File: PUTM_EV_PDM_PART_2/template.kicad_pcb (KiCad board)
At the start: 4 copper layers, 60 x 90 mm, 7 parts, among them J3 Conn_02x18_Counter_Clockwise, J4 WIRE OUT, J5 Conn_01x37

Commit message: Add files via upload
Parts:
- removed J5: Conn_01x37, 3RD_party:37 PIN DEUTSCH
- added J1: +24V IN, DPT13-4P:TE_DTP13-4P, F.Cu at (103.0, 103.5)
- added J2: UPS-08-07.0-01-L-V, UPT-08-07-01-L-V:UPS0807001LV, F.Cu at (154.8, 78.5)
- added J6: +24V OUT, UPT-02-01-01-L-V:SAMTEC_UPT-02-03.0-XX-X-V, F.Cu at (156.2, 121.7)
- added J7: UPS-08-07.0-01-L-V, UPT-08-07-01-L-V:UPS0807001LV, F.Cu at (154.8, 39.3)
- J3: footprint Connector_IDC:IDC-Header_2x20-1MP_P2.54mm_Latch6.5mm_Vertical -> 3RD_party:37 PIN DEUTSCH
- J4: value WIRE OUT -> Conn_01x06_Pin; footprint Connector_Wire:SolderWire-0.75sqmm_1x02_P4.8mm_D1.25mm_OD2.3mm_Relief -> Connector_IDC:IDC-Header_2x03_P2.54mm_Vertical
- moved J4 102.5 mm to (123.3, 32.0), turned to -90 degrees
- moved J3 56.7 mm to (121.4, 55.1)
- moved xd1 54.1 mm to (142.5, 35.0)
- moved xd2 49.0 mm to (104.0, 35.0)
- moved xd4 44.2 mm to (143.5, 125.5)
- moved xd3 39.1 mm to (105.2, 125.0)
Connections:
- J3 pad 15: /DASH 24VDC -> /BRAKE BALANCE 24VDC
- J3 pad 17: /PC 24VDC 4 -> /PC 24VDC 3
- J3 pad 19: /TSAL LOGIC 24VDC -> /BSPD 24VDC
- J3 pad 20: /TSAL LIGHT 24VDC -> /BSPD 24VDC
- J3 pad 21: /DIAGPORT 24VDC -> /AIR PRESSURE 24VDC
- J3 pad 22: /IR CAMS REAR 24VDC -> /AIR PRESSURE 24VDC
- J3 pad 24: /ODRIVE 3 24VDC -> /ODRIVE 2 24VDC
- J3 pad 26: /ODRIVE 5 24VDC -> /ODRIVE 4 24VDC
- J3 pad 27: /PC 24VDC 2 -> /PC 24VDC 1
- J3 pad 28: /FRONT BOX 24VDC -> /BRAKE BALANCE 24VDC
- J3 pad 3: /REARBOX 2 24VDC -> /REARBOX 1 24VDC
- J3 pad 30: /INVERTER 2 24VDC -> /INVERTER 1 24VDC
- J3 pad 33: /HV LOGIKA 2 24VDC -> /HV LOGIKA 1 24VDC
- J3 pad 6: /IR CAMS FRONT 24VDC -> /AIR PRESSURE 24VDC
- J3 pad 8: /REARBOX 4 24VDC -> /REARBOX 3 24VDC
- J3 pad 9: /SDC SOURCE -> /ASMS SOURCE
- J4 pad 1: /+24V -> /CAN_L
- J4 pad 2: /GND -> /CAN_H
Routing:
- added copper zone on In1.Cu, net (none)
- added copper zone on In2.Cu, net (none)
- added copper zone on F.Cu, net /AIR PRESSURE 24VDC
- added copper zone on In2.Cu, net /ASMS IN
- added copper zone on In2.Cu, net /ASMS SOURCE
- added copper zone on F.Cu, net /BRAKE BALANCE 24VDC
- added copper zone on In1.Cu, net /CAN_L
- added copper zone on B.Cu, net /ODRIVE 4 24VDC
- removed copper zone on B.Cu, net /ASMS IN
- removed copper zone on F.Cu, net /ASMS IN
- removed copper zone on F.Cu, net /ASMS SOURCE
- removed copper zone on B.Cu, net /CAN_H
- removed copper zone on B.Cu, net /CAN_L
- removed copper zone on F.Cu, net /DASH 24VDC
- removed copper zone on F.Cu, net /DIAGPORT 24VDC
- removed copper zone on F.Cu, net /HV LOGIKA 1 24VDC
- removed copper zone on B.Cu, net /ODRIVE 2 24VDC
- removed copper zone on B.Cu, net /ODRIVE 5 24VDC
- removed copper zone on F.Cu, net /PC 24VDC 1
- removed copper zone on B.Cu, net /REARBOX 1 24VDC
- removed copper zone on B.Cu, net /REARBOX 3 24VDC
- removed copper zone on B.Cu, net /REARBOX 5 24VDC
- removed copper zone on B.Cu, net /TSAL LIGHT 24VDC
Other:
- board size 60 x 90 mm -> 60 x 100 mm

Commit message: Add files via upload
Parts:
- removed J1: +24V IN, DPT13-4P:TE_DTP13-4P
- removed J6: +24V OUT, UPT-02-01-01-L-V:SAMTEC_UPT-02-03.0-XX-X-V
- added J5: +24V OUT, UPT-02-01-01-L-V:SAMTEC_UPT-02-03.0-XX-X-V, F.Cu at (154.1, 119.1)
- added J8: +24V IN, DPT13-4P:TE_DTP13-4P, F.Cu at (107.4, 101.6)
- J4: value Conn_01x06_Pin -> Conn_01x06
- moved J7 3.12 mm to (153.8, 36.3)
- moved J2 2.93 mm to (153.8, 75.8)
- moved xd4 1.84 mm to (141.8, 126.2)
- moved xd1 1.12 mm to (142.0, 34.0)
- moved J4 0.10 mm to (123.4, 32.1)
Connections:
- J2 pad G1: /INVERTER 1 24VDC -> /PC 24VDC 3
- J2 pad G2: /INVERTER 1 24VDC -> /PC 24VDC 3
- J2 pad G3: /INVERTER 1 24VDC -> /PC 24VDC 3
- J2 pad G4: /INVERTER 1 24VDC -> /PC 24VDC 3
- J2 pad G5: /INVERTER 1 24VDC -> /PC 24VDC 3
- J2 pad G6: /INVERTER 1 24VDC -> /PC 24VDC 3
- J2 pad H1: /PC 24VDC 3 -> /INVERTER 1 24VDC
- J2 pad H2: /PC 24VDC 3 -> /INVERTER 1 24VDC
- J2 pad H3: /PC 24VDC 3 -> /INVERTER 1 24VDC
- J2 pad H4: /PC 24VDC 3 -> /INVERTER 1 24VDC
- J2 pad H5: /PC 24VDC 3 -> /INVERTER 1 24VDC
- J2 pad H6: /PC 24VDC 3 -> /INVERTER 1 24VDC
- J7 pad F1: /ODRIVE 2 24VDC -> /PC 24VDC 5
- J7 pad F2: /ODRIVE 2 24VDC -> /PC 24VDC 5
- J7 pad F3: /ODRIVE 2 24VDC -> /PC 24VDC 5
- J7 pad F4: /ODRIVE 2 24VDC -> /PC 24VDC 5
- J7 pad F5: /ODRIVE 2 24VDC -> /PC 24VDC 5
- J7 pad F6: /ODRIVE 2 24VDC -> /PC 24VDC 5
- J7 pad G1: /PC 24VDC 5 -> /ODRIVE 2 24VDC
- J7 pad G2: /PC 24VDC 5 -> /ODRIVE 2 24VDC
- J7 pad G3: /PC 24VDC 5 -> /ODRIVE 2 24VDC
- J7 pad G4: /PC 24VDC 5 -> /ODRIVE 2 24VDC
- J7 pad G5: /PC 24VDC 5 -> /ODRIVE 2 24VDC
- J7 pad G6: /PC 24VDC 5 -> /ODRIVE 2 24VDC
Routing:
- added copper zone on F.Cu, net /+24V
- added copper zone on F.Cu, net /ASMS SOURCE
- added copper zone on B.Cu, net /BSPD 24VDC
- added copper zone on In2.Cu, net /CAN_H
- added copper zone on F.Cu, net /GND
- added copper zone on B.Cu, net /HV LOGIKA 1 24VDC
- added copper zone on In1.Cu, net /ODRIVE 2 24VDC
- added copper zone on F.Cu, net /PC 24VDC 1
- added copper zone on B.Cu, net /PC 24VDC 5
- added copper zone on F.Cu, net /REARBOX 1 24VDC
- added copper zone on F.Cu, net /REARBOX 3 24VDC
- added copper zone on F.Cu, net /REARBOX 5 24VDC
- removed copper zone on B.Cu, net (none)
- removed copper zone on F.Cu, net (none)
- removed copper zone on In1.Cu, net (none)
- removed copper zone on In2.Cu, net (none)
- removed copper zone on In2.Cu, net /ASMS SOURCE

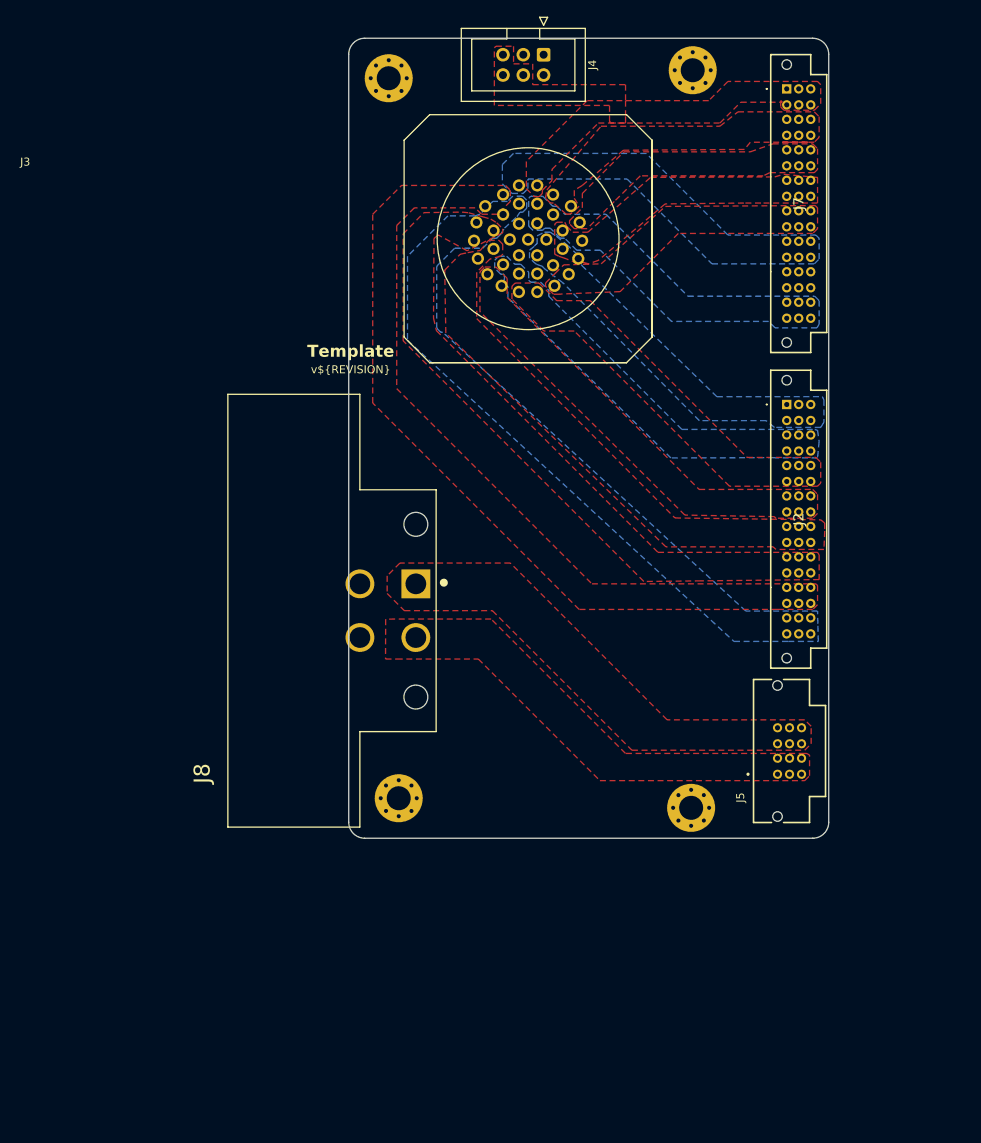
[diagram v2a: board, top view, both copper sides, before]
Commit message: Removed ODRIVE
+fixed copper plates
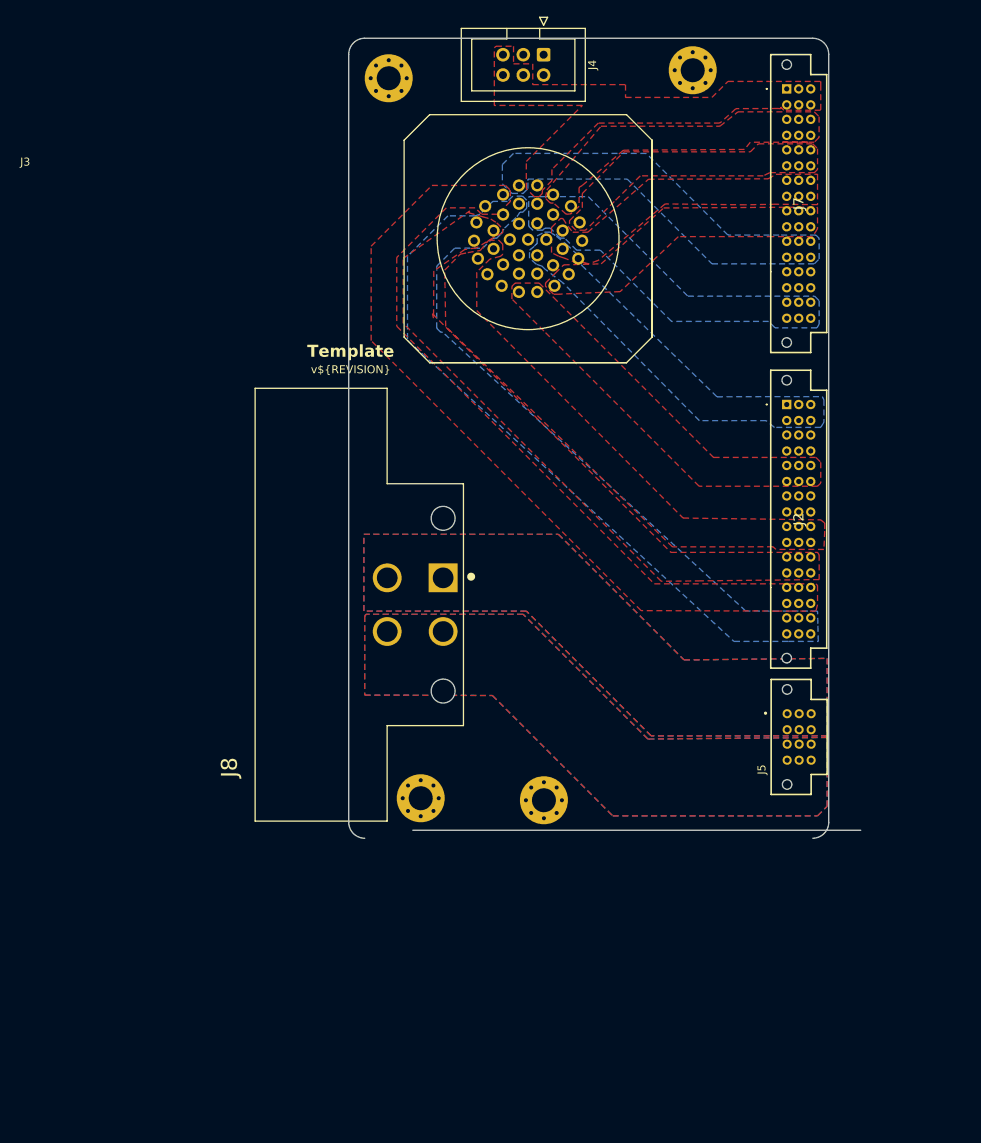
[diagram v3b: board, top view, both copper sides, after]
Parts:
- J5: footprint UPT-02-01-01-L-V:SAMTEC_UPT-02-03.0-XX-X-V -> UPS-02-04.0-01-L-V:SAMTEC_UPS-02-04.0-01-L-V
- moved xd4 18.4 mm to (123.4, 125.2)
- moved J8 3.49 mm to (110.8, 100.8)
- moved xd3 2.75 mm to (108.0, 125.0)
- moved J5 1.78 mm to (153.8, 117.3)
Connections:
- J2 pad B1: /ODRIVE 4 24VDC -> Net-(J2-PadB1)
- J2 pad B2: /ODRIVE 4 24VDC -> Net-(J2-PadB1)
- J2 pad B3: /ODRIVE 4 24VDC -> Net-(J2-PadB1)
- J2 pad B4: /ODRIVE 4 24VDC -> Net-(J2-PadB1)
- J2 pad B5: /ODRIVE 4 24VDC -> Net-(J2-PadB1)
- J2 pad B6: /ODRIVE 4 24VDC -> Net-(J2-PadB1)
- J2 pad D1: /ODRIVE 1 24VDC -> Net-(J2-PadD1)
- J2 pad D2: /ODRIVE 1 24VDC -> Net-(J2-PadD1)
- J2 pad D3: /ODRIVE 1 24VDC -> Net-(J2-PadD1)
- J2 pad D4: /ODRIVE 1 24VDC -> Net-(J2-PadD1)
- J2 pad D5: /ODRIVE 1 24VDC -> Net-(J2-PadD1)
- J2 pad D6: /ODRIVE 1 24VDC -> Net-(J2-PadD1)
- J3 pad 24: /ODRIVE 2 24VDC -> /ODRIVE 3 24VDC
- J3 pad 26: /ODRIVE 4 24VDC -> /ODRIVE 5 24VDC
- J5 pad P01_1: /GND -> /+24V
- J5 pad P01_2: /GND -> /+24V
- J5 pad P01_3: /GND -> /+24V
- J5 pad P01_4: /GND -> /+24V
- J5 pad P01_5: /GND -> /+24V
- J5 pad P01_6: /GND -> /+24V
- J5 pad P02_1: /+24V -> /GND
- J5 pad P02_2: /+24V -> /GND
- J5 pad P02_3: /+24V -> /GND
- J5 pad P02_4: /+24V -> /GND
- J5 pad P02_5: /+24V -> /GND
- J5 pad P02_6: /+24V -> /GND
- J7 pad G1: /ODRIVE 2 24VDC -> Net-(J7-PadG1)
- J7 pad G2: /ODRIVE 2 24VDC -> Net-(J7-PadG1)
- J7 pad G3: /ODRIVE 2 24VDC -> Net-(J7-PadG1)
- J7 pad G4: /ODRIVE 2 24VDC -> Net-(J7-PadG1)
- J7 pad G5: /ODRIVE 2 24VDC -> Net-(J7-PadG1)
- J7 pad G6: /ODRIVE 2 24VDC -> Net-(J7-PadG1)
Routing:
- net /CAN_L: track 0.00 -> 25.1 mm
- net /CAN_H: track 0.00 -> 20.8 mm
- added copper zone on B.Cu, net /+24V
- added copper zone on In1.Cu, net /+24V
- added copper zone on In2.Cu, net /+24V
- added copper zone on B.Cu, net /GND
- added copper zone on In1.Cu, net /GND
- added copper zone on In2.Cu, net /GND
- removed copper zone on In2.Cu, net /CAN_H
- removed copper zone on In1.Cu, net /CAN_L
- removed copper zone on F.Cu, net /ODRIVE 1 24VDC
- removed copper zone on In1.Cu, net /ODRIVE 2 24VDC
- removed copper zone on B.Cu, net /ODRIVE 4 24VDC
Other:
- board size 60 x 100 mm -> 64 x 100 mm

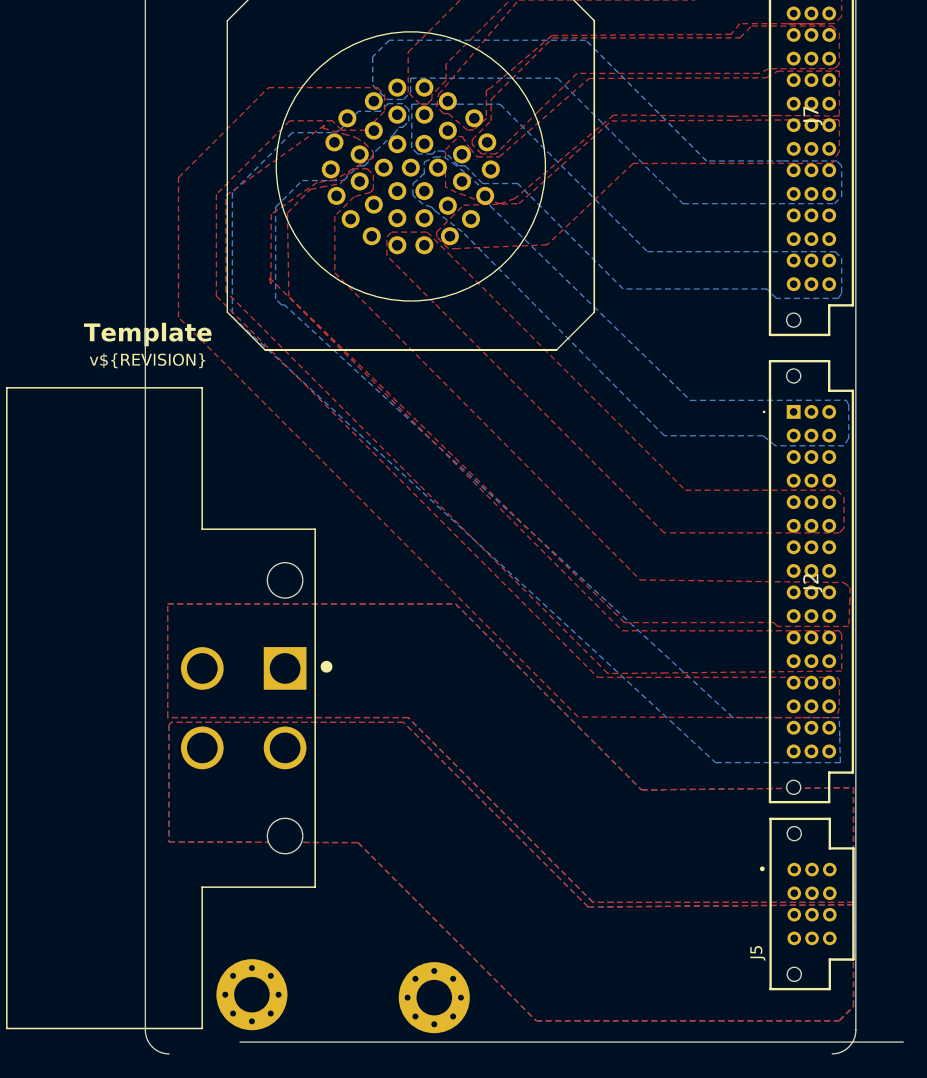
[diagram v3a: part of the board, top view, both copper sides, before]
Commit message: Added Fan and pump support.
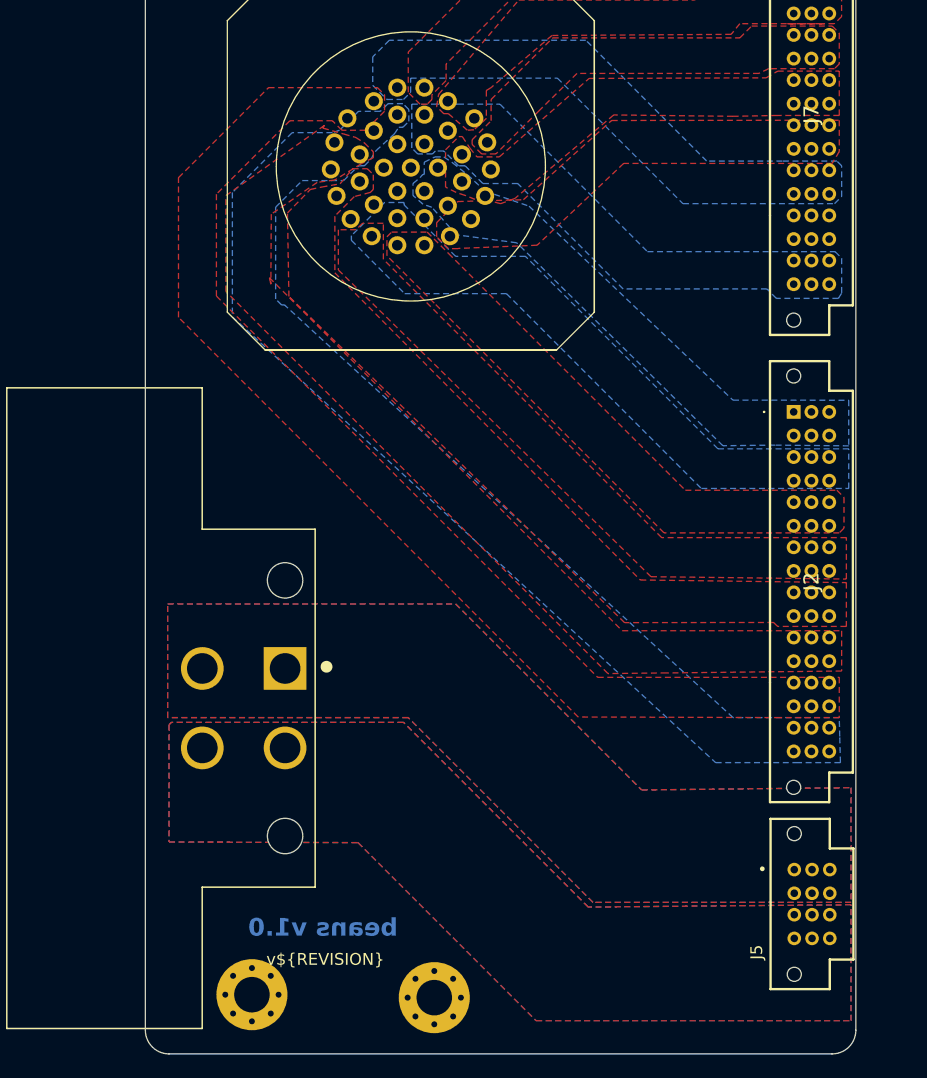
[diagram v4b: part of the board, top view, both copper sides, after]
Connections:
- J2 pad B1: Net-(J2-PadB1) -> /PUMP_1
- J2 pad B2: Net-(J2-PadB1) -> /PUMP_1
- J2 pad B3: Net-(J2-PadB1) -> /PUMP_1
- J2 pad B4: Net-(J2-PadB1) -> /PUMP_1
- J2 pad B5: Net-(J2-PadB1) -> /PUMP_1
- J2 pad B6: Net-(J2-PadB1) -> /PUMP_1
- J2 pad D1: Net-(J2-PadD1) -> /PUMP_2
- J2 pad D2: Net-(J2-PadD1) -> /PUMP_2
- J2 pad D3: Net-(J2-PadD1) -> /PUMP_2
- J2 pad D4: Net-(J2-PadD1) -> /PUMP_2
- J2 pad D5: Net-(J2-PadD1) -> /PUMP_2
- J2 pad D6: Net-(J2-PadD1) -> /PUMP_2
- J3 pad 11: unconnected-(J3-Pin_11-Pad11) -> /PUMP_2
- J3 pad 12: /ODRIVE 1 24VDC -> unconnected-(J3-Pin_12-Pad12)
- J3 pad 23: /ODRIVE 2 24VDC -> /FAN
- J3 pad 24: /ODRIVE 3 24VDC -> unconnected-(J3-Pin_24-Pad24)
- J3 pad 25: /ODRIVE 4 24VDC -> /PUMP_1
- J3 pad 26: /ODRIVE 5 24VDC -> unconnected-(J3-Pin_26-Pad26)
- J5 pad P01_1: /+24V -> (no net)
- J5 pad P01_2: /+24V -> (no net)
- J5 pad P01_3: /+24V -> (no net)
- J5 pad P01_4: /+24V -> (no net)
- J5 pad P01_5: /+24V -> (no net)
- J5 pad P01_6: /+24V -> (no net)
- J5 pad P02_1: /GND -> (no net)
- J5 pad P02_2: /GND -> (no net)
- J5 pad P02_3: /GND -> (no net)
- J5 pad P02_4: /GND -> (no net)
- J5 pad P02_5: /GND -> (no net)
- J5 pad P02_6: /GND -> (no net)
- J7 pad G1: Net-(J7-PadG1) -> /FAN
- J7 pad G2: Net-(J7-PadG1) -> /FAN
- J7 pad G3: Net-(J7-PadG1) -> /FAN
- J7 pad G4: Net-(J7-PadG1) -> /FAN
- J7 pad G5: Net-(J7-PadG1) -> /FAN
- J7 pad G6: Net-(J7-PadG1) -> /FAN
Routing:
- net /ASMS IN: track 0.00 -> 25.9 mm
- added copper zone on In2.Cu, net /FAN
- added copper zone on B.Cu, net /PUMP_1
- added copper zone on F.Cu, net /PUMP_2
- removed copper zone on In2.Cu, net /ASMS IN
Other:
- board size 64 x 100 mm -> 60 x 100 mm
- board text added: "beans v1.0"
- board text removed: "Template"
